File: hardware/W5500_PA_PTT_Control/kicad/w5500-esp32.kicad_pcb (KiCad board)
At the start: 2 copper layers, 18 parts, among them J1 ESP32_DevKitC_Socket_40P_25.4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, Q1 2SC1815, Q3 2SC1815, Q5 2SJ334, U1 TA48033S, U2 L7805

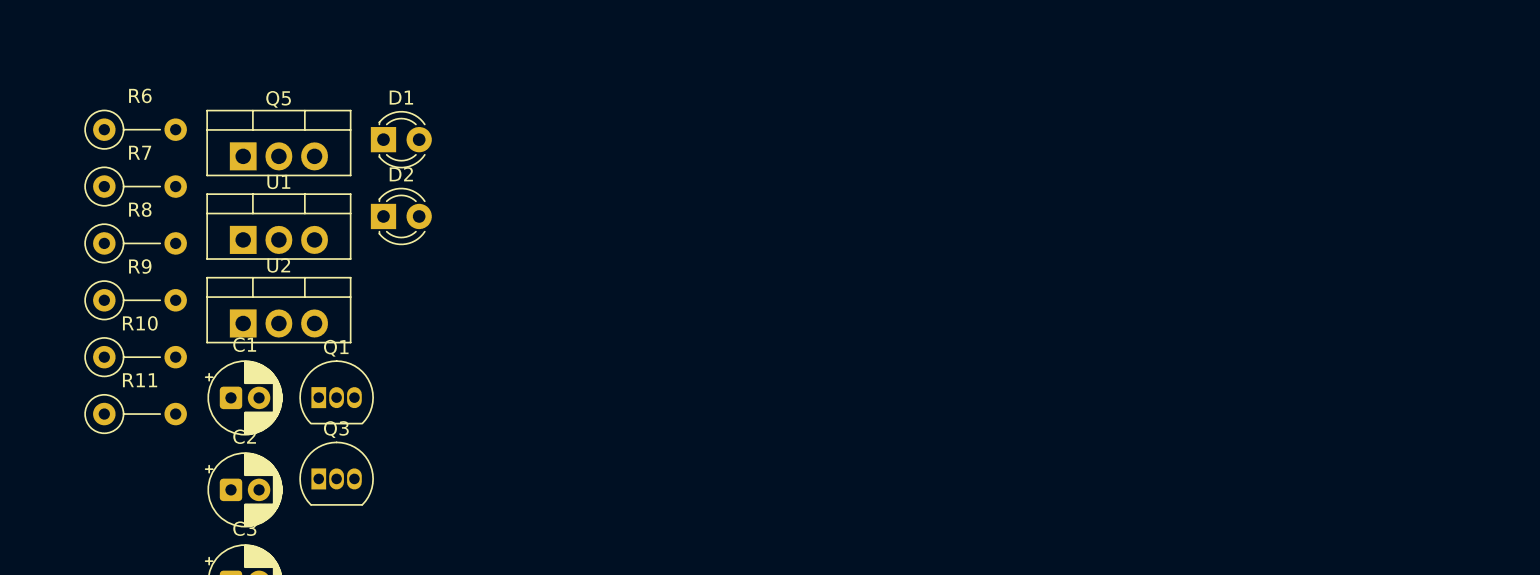
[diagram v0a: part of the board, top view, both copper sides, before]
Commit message: W5500制御基板: R8を1kΩに、R12(Q1ベースのプルダウン)追加、Q5の足番号修正、放熱器を追加
- R8(Q5ゲートのプルアップ)を100Ωから1kΩ(1/2W推奨)へ。Q1 ON中の電流を約12〜14mAに抑える
- Q1のベースをGNDへプルダウンするR12(10kΩ)を追加(GPIO26が確定しない間もQ1をOFFに保つ)
- Q5のシンボルを端子番号1=G・2=D・3=Sのproject_symbols:2SJ334に変更
  (従来のDevice:Q_PMOSは端子番号D/G/Sで、基板データ上Q5が未接続になっていた)
- U1・U2・Q5に放熱器(秋月[105054] 20×20×25mm)。基板データでTO-220の3部品を25mm間隔に配置
- 仕様書(Rev.2.4)・接続一覧(日英・Word・PDF)、回路図PDF/SVGを更新
- ERCの件数は変更前と同じ(15件)。DRCの回路図一致チェックでR8の値とQ5のパッド未接続が解消

Co-Authored-By: Claude Opus 5.5 <noreply@anthropic.com>
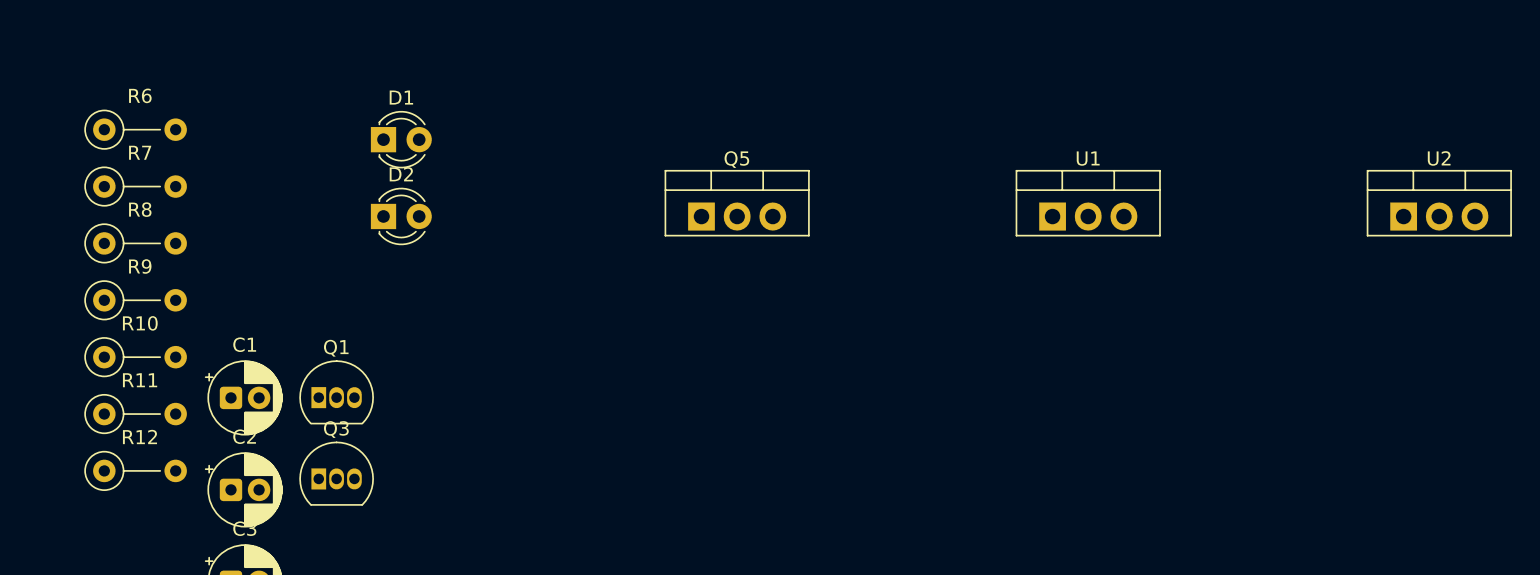
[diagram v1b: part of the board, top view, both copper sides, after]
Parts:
- added R12: 10k, Resistor_THT:R_Axial_DIN0207_L6.3mm_D2.5mm_P5.08mm_Vertical, F.Cu at (132.5, 178.1)
- R8: value 10k -> 1k
- moved U2 83.0 mm to (225.0, 160.0)
- moved U1 57.7 mm to (200.0, 160.0)
- moved Q5 32.9 mm to (175.0, 160.0)
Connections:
- Q5 pad 1: (no net) -> Net-(Q1-C)
- Q5 pad 2: (no net) -> /Power
- Q5 pad 3: (no net) -> +12V
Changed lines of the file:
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@@
 	(footprint "Package_TO_SOT_THT:TO-220-3_Vertical"
 		(layer "F.Cu")
-		(at 142.365 167.615)
+		(at 225.0 160.0)
 		(descr "TO-220-3, Vertical, RM 2.54mm, see https://www.vishay.com/docs/66542/to-220-1.pdf")
 		(tags "TO-220-3 Vertical RM 2.54mm")
@@
 	(footprint "Package_TO_SOT_THT:TO-220-3_Vertical"
 		(layer "F.Cu")
-		(at 142.365 155.715)
+		(at 175.0 160.0)
 		(descr "TO-220-3, Vertical, RM 2.54mm, see https://www.vishay.com/docs/66542/to-220-1.pdf")
 		(tags "TO-220-3 Vertical RM 2.54mm")
@@
 			(layers "*.Cu" "*.Mask")
 			(remove_unused_layers no)
+			(net "Net-(Q1-C)")
+			(pinfunction "G")
+			(pintype "input")
 		)
 		(pad "2" thru_hole oval
@@
 			(layers "*.Cu" "*.Mask")
 			(remove_unused_layers no)
+			(net "/Power")
+			(pinfunction "D")
+			(pintype "passive")
 		)
 		(pad "3" thru_hole oval
@@
 			(layers "*.Cu" "*.Mask")
 			(remove_unused_layers no)
+			(net "+12V")
+			(pinfunction "S")
+			(pintype "passive")
 		)
 		(embedded_fonts no)
@@
 			(remove_unused_layers no)
 			(net "Net-(Q1-B)")
+			(pintype "passive")
+		)
+		(embedded_fonts no)
+		(model "${KICAD10_3DMODEL_DIR}/Resistor_THT.3dshapes/R_Axial_DIN0207_L6.3mm_D2.5mm_P5.08mm_Vertical.step"
+			(offset
+				(xyz 0 0 0)
+			)
+			(scale
+				(xyz 1 1 1)
+			)
+			(rotate
+				(xyz 0 0 0)
+			)
+		)
+	)
+	(footprint "Resistor_THT:R_Axial_DIN0207_L6.3mm_D2.5mm_P5.08mm_Vertical"
+		(layer "F.Cu")
+		(at 132.475 178.115)
+		(descr "Resistor, Axial_DIN0207 series, Axial, Vertical, pin pitch=5.08mm, 0.25W = 1/4W, length*diameter=6.3*2.5mm^2, http://cdn-reichelt.de/documents/datenblatt/B400/1_4W%23YAG.pdf")
+		(tags "Resistor Axial_DIN0207 series Axial Vertical pin pitch 5.08mm 0.25W = 1/4W length 6.3mm diameter 2.5mm")
+		(property "Reference" "R12"
+			(at 2.54 -2.37 0)
+			(layer "F.SilkS")
+			(effects
+				(font
+					(size 1 1)
+					(thickness 0.15)
+				)
+			)
+		)
+		(property "Value" "10k"
+			(at 2.54 2.37 0)
+			(layer "F.Fab")
+			(effects
+				(font
+					(size 1 1)
+					(thickness 0.15)
+				)
+			)
+		)
+		(property "Datasheet" ""
+			(at 0 0 0)
+			(layer "F.Fab")
+			(hide yes)
+			(effects
+				(font
+					(size 1.27 1.27)
+				)
+			)
+		)
+		(property "Description" ""
+			(at 0 0 0)
+			(layer "F.Fab")
+			(hide yes)
+			(effects
+				(font
+					(size 1.27 1.27)
+				)
+			)
+		)
+		(property "KiLib_Generator" "resistor/THT"
+			(at 0 0 0)
+			(layer "F.SilkS")
+			(hide yes)
+			(effects
+				(font
+					(size 1 1)
+					(thickness 0.15)
+				)
+			)
+		)
+		(property ki_fp_filters "R_*")
+		(sheetname "/")
+		(sheetfile "w5500-esp32.kicad_sch")
+		(units
+			(unit
+				(name "A")
+				(pins "1" "2")
+			)
+		)
+		(attr through_hole)
+		(duplicate_pad_numbers_are_jumpers no)
+		(fp_line
+			(start 1.37 0)
+			(end 3.98 0)
+			(stroke
+				(width 0.12)
+				(type solid)
+			)
+			(layer "F.SilkS")
+		)
+		(fp_circle
+			(center 0 0)
+			(end 1.37 0)
+			(stroke
+				(width 0.12)
+				(type solid)
+			)
+			(fill no)
+			(layer "F.SilkS")
+		)
+		(fp_rect
+			(start -1.5 -1.5)
+			(end 6.13 1.5)
+			(stroke
+				(width 0.05)
+				(type solid)
+			)
+			(fill no)
+			(layer "F.CrtYd")
+		)
+		(fp_line
+			(start 0 0)
+			(end 5.08 0)
+			(stroke
+				(width 0.1)
+				(type solid)
+			)
+			(layer "F.Fab")
+		)
+		(fp_circle
+			(center 0 0)
+			(end 1.25 0)
+			(stroke
+				(width 0.1)
+				(type solid)
+			)
+			(fill no)
+			(layer "F.Fab")
+		)
+		(fp_text user "${REFERENCE}"
+			(at 2.54 -2.37 0)
+			(layer "F.Fab")
+			(effects
+				(font
+					(size 1 1)
+					(thickness 0.15)
+				)
+			)
+		)
+		(pad "1" thru_hole circle
+			(at 0 0)
+			(size 1.6 1.6)
+			(drill 0.8)
+			(layers "*.Cu" "*.Mask")
+			(remove_unused_layers no)
+			(net "Net-(Q1-B)")
+			(pintype "passive")
+		)
+		(pad "2" thru_hole circle
+			(at 5.08 0)
+			(size 1.6 1.6)
+			(drill 0.8)
+			(layers "*.Cu" "*.Mask")
+			(remove_unused_layers no)
+			(net "GND")
 			(pintype "passive")
 		)
@@
 	(footprint "Package_TO_SOT_THT:TO-220-3_Vertical"
 		(layer "F.Cu")
-		(at 142.365 161.665)
+		(at 200.0 160.0)
 		(descr "TO-220-3, Vertical, RM 2.54mm, see https://www.vishay.com/docs/66542/to-220-1.pdf")
 		(tags "TO-220-3 Vertical RM 2.54mm")
@@
 			)
 		)
-		(property "Value" "10k"
+		(property "Value" "1k"
 			(at 2.54 2.37 0)
 			(layer "F.Fab")

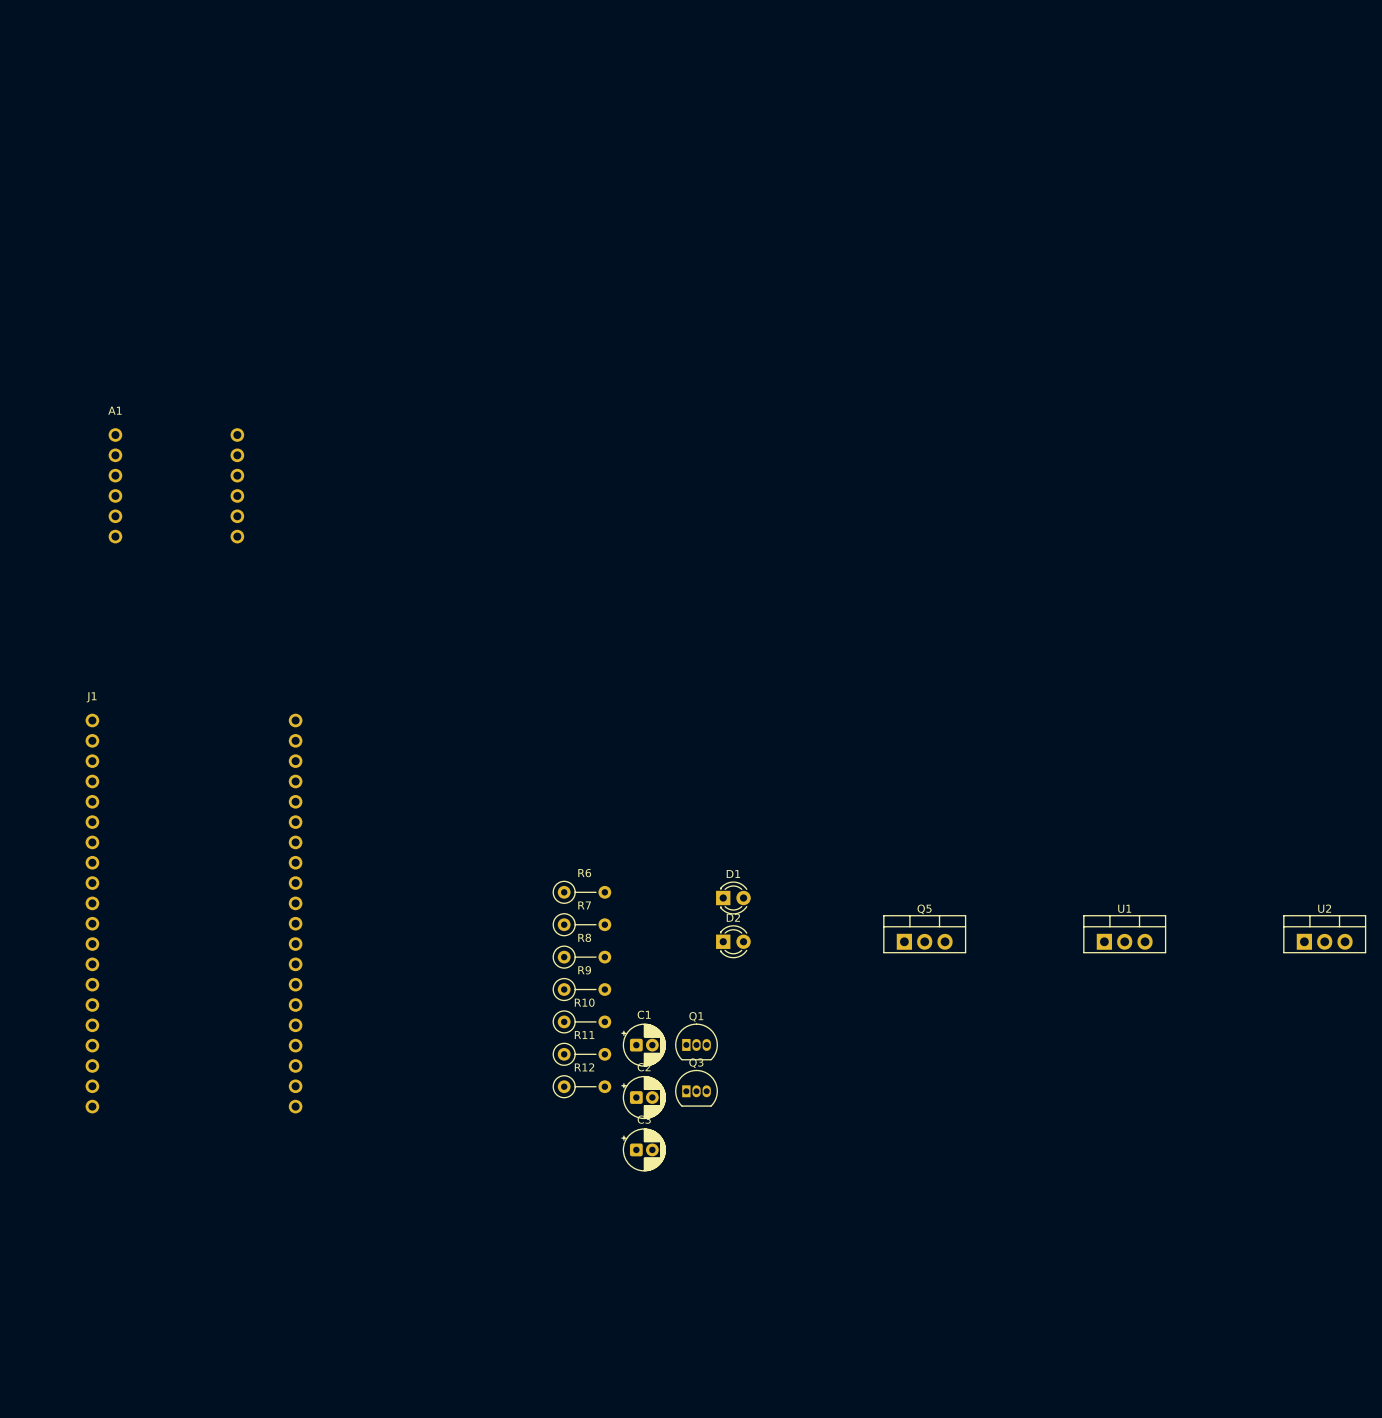
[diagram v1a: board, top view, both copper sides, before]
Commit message: W5500制御基板の外形を115×72mmにして部品を配置
- Edge.Cutsに115×72mmの外形線を追加
- 全部品を外形内に配置。TO-220(U1・U2・Q5)は下辺に沿って23mm間隔、放熱タブを下端側に向け、
  放熱器(20×20mm)の範囲をDwgs.Userに記入。J2/J5/J6用の場所を右端に確保(フットプリント未指定)
- DRC違反0件(未配線とJ2/J5/J6未指定、既存のGND<NO NET>を除く)
- 仕様書(日英・Word・PDF)の放熱器の節に基板外形と配置を追記

Co-Authored-By: Claude Opus 5.5 <noreply@anthropic.com>
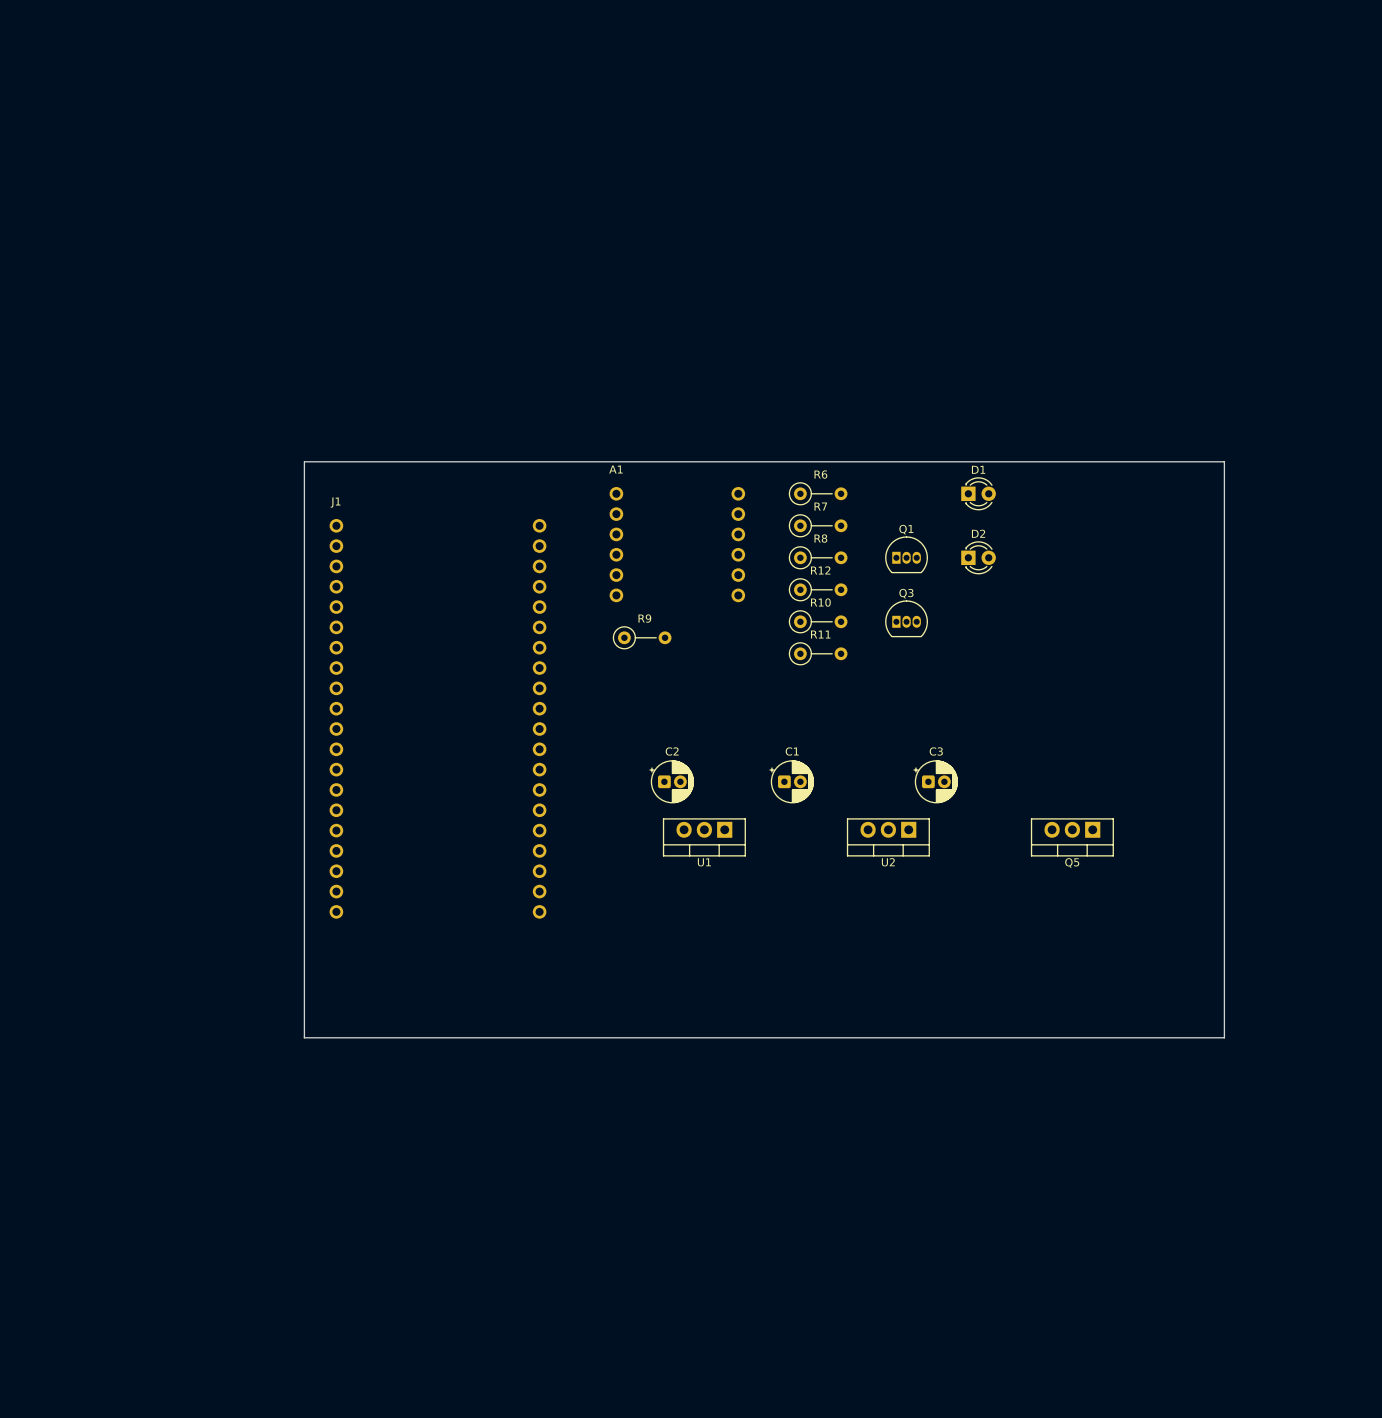
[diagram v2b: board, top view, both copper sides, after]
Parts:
- moved R12 68.8 mm to (162.0, 116.0)
- moved Q1 66.3 mm to (174.0, 112.0)
- moved Q3 64.3 mm to (174.0, 120.0)
- moved A1 63.0 mm to (139.0, 104.0)
- moved D1 59.1 mm to (183.0, 104.0)
- moved C3 58.7 mm to (178.0, 140.0)
- moved R11 58.1 mm to (162.0, 124.0)
- moved R10 58.1 mm to (162.0, 120.0)
- moved R8 58.0 mm to (162.0, 112.0)
- moved R7 58.0 mm to (162.0, 108.0)
- moved R6 57.9 mm to (162.0, 104.0)
- moved D2 56.9 mm to (183.0, 112.0)
- moved U2 51.4 mm to (175.5, 146.0), turned to 180 degrees
- moved U1 49.5 mm to (152.5, 146.0), turned to 180 degrees
- moved R9 44.6 mm to (140.0, 122.0)
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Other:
- board outline added: 115 x 72 mm
- board text added: "J2/J5/J6"
- board text added: "放熱器 Q5 20x20"
- board text added: "放熱器 U1 20x20"
- board text added: "放熱器 U2 20x20"
